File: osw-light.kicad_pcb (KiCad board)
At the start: 2 copper layers, 34.9 x 36.2 mm, 56 parts, among them J1 Conn_01x02, J2 USB_C_Receptacle_USB2.0, J3 Conn_01x02, J4 Conn_01x04, J5 Conn_01x04, Q1 2N7002, SW1 SW_Push, SW2 SW_Push, SW4 SW_Push, SW5 SW_Push, U1 DS3231MZ, U10 XC6209, U11 MCP73831T-2ACI_OT, U13 XC6209, U2 BMA400, U4 GC9A01_IPS_display, U6 CH340E, U7 ttgo-32-micro, U9 TPS2115A

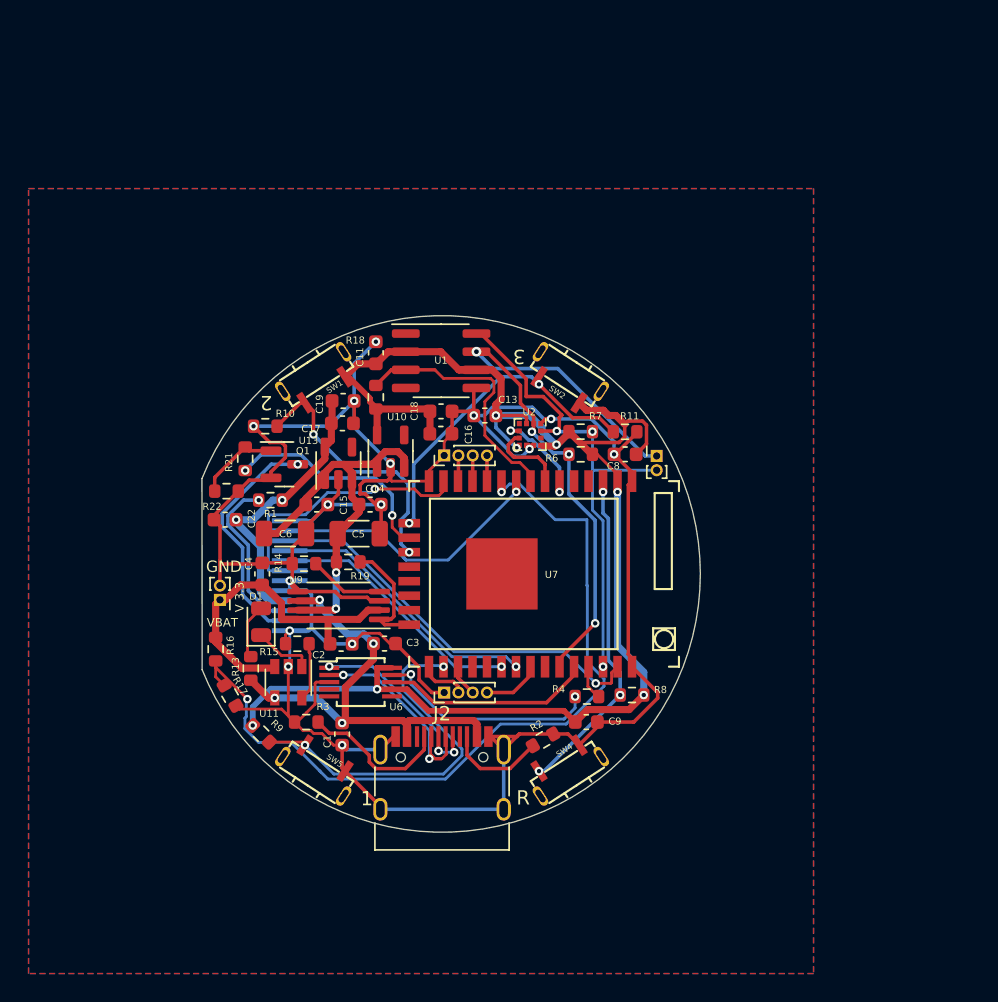
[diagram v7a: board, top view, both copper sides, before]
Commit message: edit files a bit, also I wanted to learn how to length-match traces, so now data lines are equal length :)
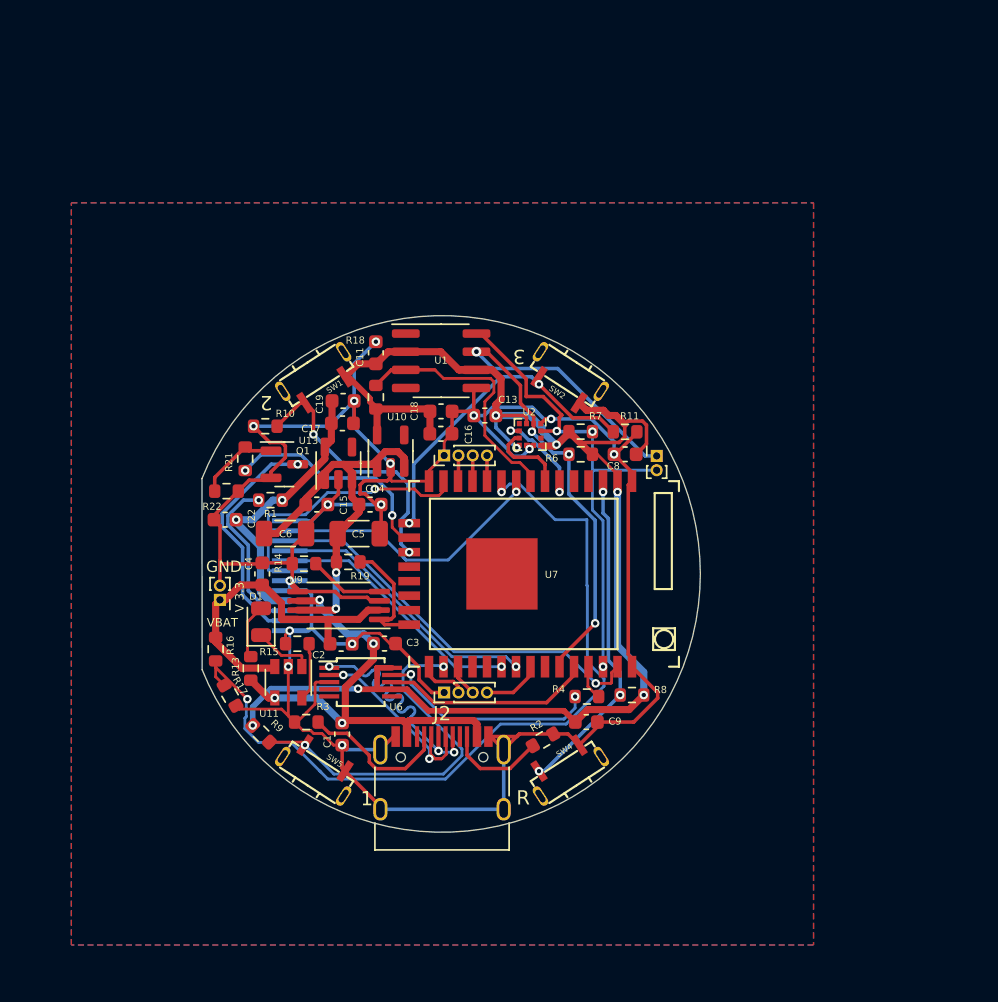
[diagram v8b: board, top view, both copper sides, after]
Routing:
- net /D_P: track 14.1 -> 18.7 mm
- net /D_N: track 15.4 -> 14.6 mm
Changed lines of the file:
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@@
   (segment (start 81.455528 118.891638) (end 80.625448 118.061558) (width 0.25) (layer "B.Cu") (net 1))
   (segment (start 82.572828 103.61752) (end 83.297348 102.893) (width 0.25) (layer "F.Cu") (net 2))
+  (segment (start 63.092346 120.042346) (end 63.12952 120.07952) (width 0.4) (layer "F.Cu") (net 2))
   (segment (start 79.179648 121.505) (end 78.305128 122.37952) (width 0.5) (layer "F.Cu") (net 2))
   (segment (start 64.420928 100.52752) (end 64.335428 100.44202) (width 0.5) (layer "F.Cu") (net 2))
@@
   (segment (start 79.099237 100.532129) (end 80.274703 100.532129) (width 0.5) (layer "F.Cu") (net 2))
   (segment (start 76.988077 102.942372) (end 76.890929 103.03952) (width 0.5) (layer "F.Cu") (net 2))
+  (segment (start 63.12952 120.07952) (end 64.421906 120.07952) (width 0.4) (layer "F.Cu") (net 2))
   (segment (start 65.201128 96.42932) (end 66.432428 96.42932) (width 0.5) (layer "F.Cu") (net 2))
   (segment (start 70.150728 97.69932) (end 71.382428 97.69932) (width 0.5) (layer "F.Cu") (net 2))
@@
   (via (at 81.266928 106.25952) (size 0.6) (drill 0.3) (layers "F.Cu" "B.Cu") (net 2))
   (via (at 83.105528 120.48312) (size 0.6) (drill 0.3) (layers "F.Cu" "B.Cu") (net 2))
-  (via (at 64.421906 120.07952) (size 0.6) (drill 0.3) (layers "F.Cu" "B.Cu") (net 2))
+  (via (at 63.092346 120.042346) (size 0.6) (drill 0.3) (layers "F.Cu" "B.Cu") (net 2))
   (via (at 74.188383 103.182065) (size 0.6) (drill 0.3) (layers "F.Cu" "B.Cu") (net 2))
   (segment (start 55.707565 121.314335) (end 55.707565 122.616157) (width 0.4) (layer "B.Cu") (net 2))
-  (segment (start 64.421906 120.07952) (end 64.382395 120.040009) (width 0.4) (layer "B.Cu") (net 2))
   (segment (start 75.966699 101.744201) (end 75.966699 101.991676) (width 0.5) (layer "B.Cu") (net 2))
   (segment (start 56.981891 120.040009) (end 55.707565 121.314335) (width 0.4) (layer "B.Cu") (net 2))
@@
   (segment (start 75.966699 101.991676) (end 76.917395 102.942372) (width 0.5) (layer "B.Cu") (net 2))
   (segment (start 72.745928 100.89952) (end 75.122018 100.89952) (width 0.5) (layer "B.Cu") (net 2))
+  (segment (start 56.981891 120.040009) (end 63.090009 120.040009) (width 0.4) (layer "B.Cu") (net 2))
   (segment (start 83.105528 120.48312) (end 83.105528 118.87812) (width 0.5) (layer "B.Cu") (net 2))
   (segment (start 83.105528 118.87812) (end 81.266928 117.03952) (width 0.5) (layer "B.Cu") (net 2))
   (segment (start 75.122018 100.89952) (end 75.966699 101.744201) (width 0.5) (layer "B.Cu") (net 2))
-  (segment (start 64.382395 120.040009) (end 56.981891 120.040009) (width 0.4) (layer "B.Cu") (net 2))
+  (segment (start 63.090009 120.040009) (end 63.092346 120.042346) (width 0.4) (layer "B.Cu") (net 2))
   (segment (start 56.874291 123.782883) (end 59.158591 123.782883) (width 0.2) (layer "F.Cu") (net 3))
   (segment (start 59.158591 123.782883) (end 59.367846 123.992138) (width 0.2) (layer "F.Cu") (net 3))
@@
   (via (at 69.819939 124.492421) (size 0.6) (drill 0.3) (layers "F.Cu" "B.Cu") (net 51))
   (segment (start 69.819939 124.492421) (end 68.811781 124.492421) (width 0.2) (layer "B.Cu") (net 51))
-  (segment (start 68.720928 124.401568) (end 68.720928 123.10712) (width 0.2) (layer "B.Cu") (net 51))
+  (segment (start 66.559707 121.397496) (end 66.559707 121.397497) (width 0.2) (layer "B.Cu") (net 51))
+  (segment (start 65.927181 121.181494) (end 65.927182 121.181494) (width 0.2) (layer "B.Cu") (net 51))
+  (segment (start 63.381593 119.06017) (end 63.381594 119.060171) (width 0.2) (layer "B.Cu") (net 51))
+  (segment (start 64.230122 119.908699) (end 64.230123 119.9087) (width 0.2) (layer "B.Cu") (net 51))
+  (segment (start 65.711178 120.548968) (end 65.502916 120.757229) (width 0.2) (layer "B.Cu") (net 51))
+  (segment (start 64.509095 118.781198) (end 64.509096 118.781199) (width 0.2) (layer "B.Cu") (net 51))
+  (segment (start 66.77571 122.030023) (end 66.775711 122.030023) (width 0.2) (layer "B.Cu") (net 51))
+  (segment (start 64.230124 119.484436) (end 64.509096 119.205463) (width 0.2) (layer "B.Cu") (net 51))
+  (segment (start 66.559707 121.397497) (end 66.351445 121.605758) (width 0.2) (layer "B.Cu") (net 51))
   (segment (start 68.811781 124.492421) (end 68.720928 124.401568) (width 0.2) (layer "B.Cu") (net 51))
-  (segment (start 68.720928 123.10712) (end 64.093826 118.480018) (width 0.2) (layer "B.Cu") (net 51))
-  (segment (start 64.093826 118.480018) (end 61.070928 118.480018) (width 0.2) (layer "B.Cu") (net 51))
+  (segment (start 64.93336 119.629728) (end 64.654387 119.9087) (width 0.2) (layer "B.Cu") (net 51))
+  (segment (start 64.230123 119.484436) (end 64.230124 119.484436) (width 0.2) (layer "B.Cu") (net 51))
+  (segment (start 65.711178 120.548967) (end 65.711178 120.548968) (width 0.2) (layer "B.Cu") (net 51))
+  (segment (start 68.720928 124.399505) (end 66.775711 122.454288) (width 0.2) (layer "B.Cu") (net 51))
+  (segment (start 66.775711 122.030023) (end 66.983972 121.821761) (width 0.2) (layer "B.Cu") (net 51))
+  (segment (start 65.927181 121.605758) (end 65.927182 121.605759) (width 0.2) (layer "B.Cu") (net 51))
+  (segment (start 63.381594 119.060171) (end 62.801441 118.480018) (width 0.2) (layer "B.Cu") (net 51))
+  (segment (start 62.801441 118.480018) (end 61.070928 118.480018) (width 0.2) (layer "B.Cu") (net 51))
+  (segment (start 65.078652 120.757229) (end 65.078653 120.75723) (width 0.2) (layer "B.Cu") (net 51))
+  (segment (start 64.93336 119.629727) (end 64.93336 119.629728) (width 0.2) (layer "B.Cu") (net 51))
+  (segment (start 65.078653 120.332965) (end 65.357625 120.053992) (width 0.2) (layer "B.Cu") (net 51))
+  (segment (start 65.927182 121.181494) (end 66.135443 120.973232) (width 0.2) (layer "B.Cu") (net 51))
+  (segment (start 64.230123 119.9087) (end 64.230124 119.908701) (width 0.2) (layer "B.Cu") (net 51))
+  (segment (start 64.084831 118.781198) (end 64.084831 118.781199) (width 0.2) (layer "B.Cu") (net 51))
+  (segment (start 65.357624 119.629727) (end 65.357625 119.629728) (width 0.2) (layer "B.Cu") (net 51))
+  (segment (start 65.078652 120.332965) (end 65.078653 120.332965) (width 0.2) (layer "B.Cu") (net 51))
+  (segment (start 68.720928 124.401568) (end 68.720928 124.399505) (width 0.2) (layer "B.Cu") (net 51))
+  (segment (start 64.084831 118.781199) (end 63.805858 119.060171) (width 0.2) (layer "B.Cu") (net 51))
+  (arc (start 65.927182 121.605759) (mid 65.839313 121.393627) (end 65.927181 121.181494) (width 0.2) (layer "B.Cu") (net 51))
+  (arc (start 66.135443 120.548968) (mid 65.923311 120.461099) (end 65.711178 120.548967) (width 0.2) (layer "B.Cu") (net 51))
+  (arc (start 64.509096 118.781199) (mid 64.296964 118.69333) (end 64.084831 118.781198) (width 0.2) (layer "B.Cu") (net 51))
+  (arc (start 66.135443 120.973232) (mid 66.223311 120.7611) (end 66.135443 120.548968) (width 0.2) (layer "B.Cu") (net 51))
+  (arc (start 63.805858 119.060171) (mid 63.593725 119.148039) (end 63.381593 119.06017) (width 0.2) (layer "B.Cu") (net 51))
+  (arc (start 65.502916 120.757229) (mid 65.290784 120.845097) (end 65.078652 120.757229) (width 0.2) (layer "B.Cu") (net 51))
+  (arc (start 64.509096 119.205463) (mid 64.596964 118.99333) (end 64.509095 118.781198) (width 0.2) (layer "B.Cu") (net 51))
+  (arc (start 65.078653 120.75723) (mid 64.990784 120.545098) (end 65.078652 120.332965) (width 0.2) (layer "B.Cu") (net 51))
+  (arc (start 66.351445 121.605758) (mid 66.139313 121.693626) (end 65.927181 121.605758) (width 0.2) (layer "B.Cu") (net 51))
+  (arc (start 66.775711 122.454288) (mid 66.687842 122.242156) (end 66.77571 122.030023) (width 0.2) (layer "B.Cu") (net 51))
+  (arc (start 64.654387 119.9087) (mid 64.442254 119.996568) (end 64.230122 119.908699) (width 0.2) (layer "B.Cu") (net 51))
+  (arc (start 65.357625 119.629728) (mid 65.145493 119.541859) (end 64.93336 119.629727) (width 0.2) (layer "B.Cu") (net 51))
+  (arc (start 66.983972 121.397497) (mid 66.77184 121.309628) (end 66.559707 121.397496) (width 0.2) (layer "B.Cu") (net 51))
+  (arc (start 65.357625 120.053992) (mid 65.445493 119.841859) (end 65.357624 119.629727) (width 0.2) (layer "B.Cu") (net 51))
+  (arc (start 66.983972 121.821761) (mid 67.07184 121.609629) (end 66.983972 121.397497) (width 0.2) (layer "B.Cu") (net 51))
+  (arc (start 64.230124 119.908701) (mid 64.142255 119.696569) (end 64.230123 119.484436) (width 0.2) (layer "B.Cu") (net 51))
   (segment (start 69.220928 123.39452) (end 69.270439 123.444031) (width 0.2) (layer "F.Cu") (net 52))
   (segment (start 69.270439 123.444031) (end 69.270439 124.629184) (width 0.2) (layer "F.Cu") (net 52))
@@
   (via (at 68.080928 124.951079) (size 0.6) (drill 0.3) (layers "F.Cu" "B.Cu") (net 52))
   (via (at 62.052976 119.07952) (size 0.6) (drill 0.3) (layers "F.Cu" "B.Cu") (net 52))
-  (segment (start 68.080928 122.961415) (end 64.199033 119.07952) (width 0.2) (layer "B.Cu") (net 52))
-  (segment (start 68.080928 124.951079) (end 68.080928 122.961415) (width 0.2) (layer "B.Cu") (net 52))
-  (segment (start 64.199033 119.07952) (end 62.052976 119.07952) (width 0.2) (layer "B.Cu") (net 52))
+  (segment (start 68.080928 124.253801) (end 62.906647 119.07952) (width 0.2) (layer "B.Cu") (net 52))
+  (segment (start 62.906647 119.07952) (end 62.052976 119.07952) (width 0.2) (layer "B.Cu") (net 52))
+  (segment (start 68.080928 124.951079) (end 68.080928 124.253801) (width 0.2) (layer "B.Cu") (net 52))
   (segment (start 68.058928 119.094542) (end 68.058928 118.49952) (width 0.25) (layer "F.Cu") (net 54))
   (segment (start 68.500417 119.536031) (end 68.058928 119.094542) (width 0.25) (layer "F.Cu") (net 54))
@@
     (polygon
       (pts
-        (xy 95 140)
-        (xy 40 140)
-        (xy 40 85)
-        (xy 95 85)
+        (xy 95 138)
+        (xy 43 138)
+        (xy 43 86)
+        (xy 95 86)
       )
     )
